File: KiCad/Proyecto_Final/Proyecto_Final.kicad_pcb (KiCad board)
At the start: 4 copper layers, 102 x 106.3 mm, 228 parts, among them J1 I2C1, J10 PA, J11 PD, J12 SPI4, J13 OutEn, J14 CLK_OUT0, J15 RF_IN, J2 ARM SWD, J3 USB_B_Micro, J4 Boot_Select, J5 PG, J6 PC, J7 PF, J8 PB, J9 PE, Q1 Si2301CDS, SW1 Reset, T1 2450BL05A0100, T2 B0310J50100AHF, T3 B0310J50100AHF, U1 MAX1193ETI+, U10 SKY13351, U11 SKY13351, U12 SKY13351, U13 SKY13351, U14 MAAL-010200, U2 MAX2837, U3 AMS1117-3.3, U4 USBLC6-2SC6, U5 STM32F723ZCTx, U6 5P49V5929, U7 SKY13351, U8 RFFC5072, U9 SKY13351, Y1 25MHz

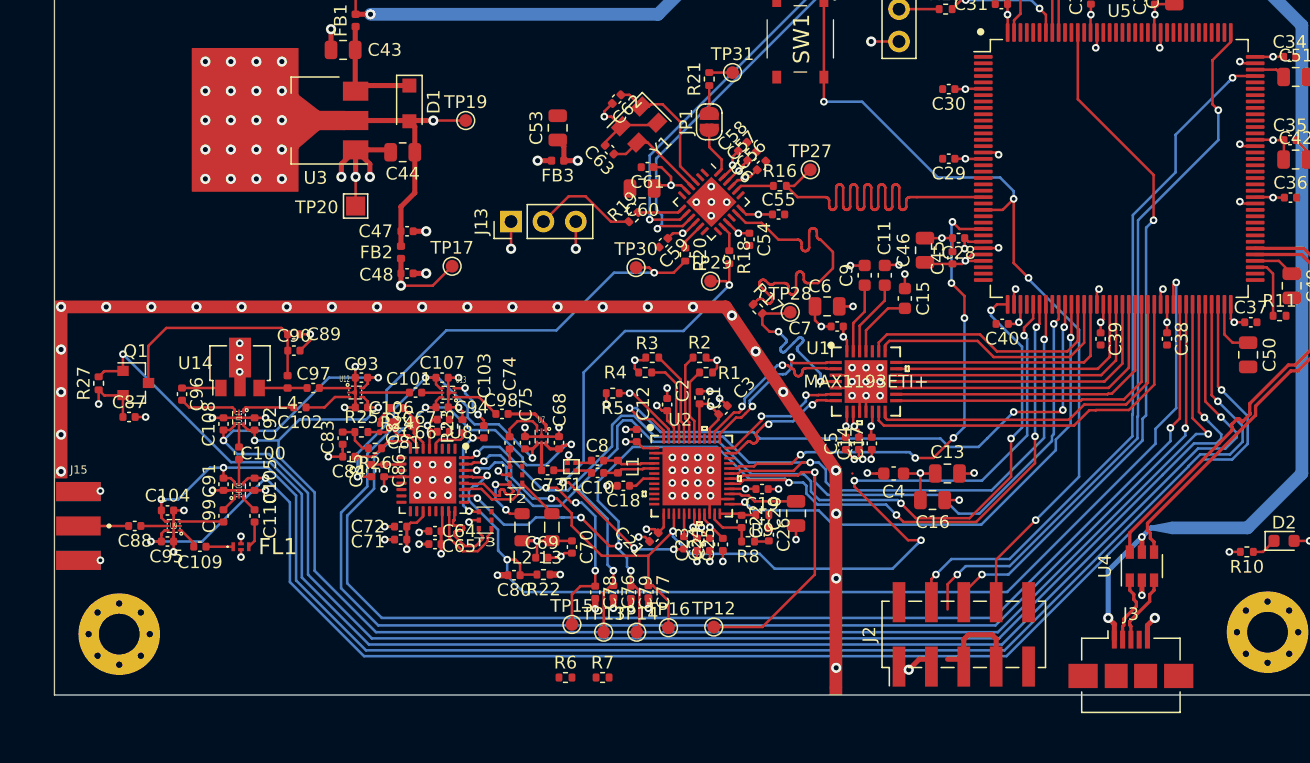
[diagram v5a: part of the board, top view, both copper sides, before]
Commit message: Pistas reacomodadas para mejor ruteo.
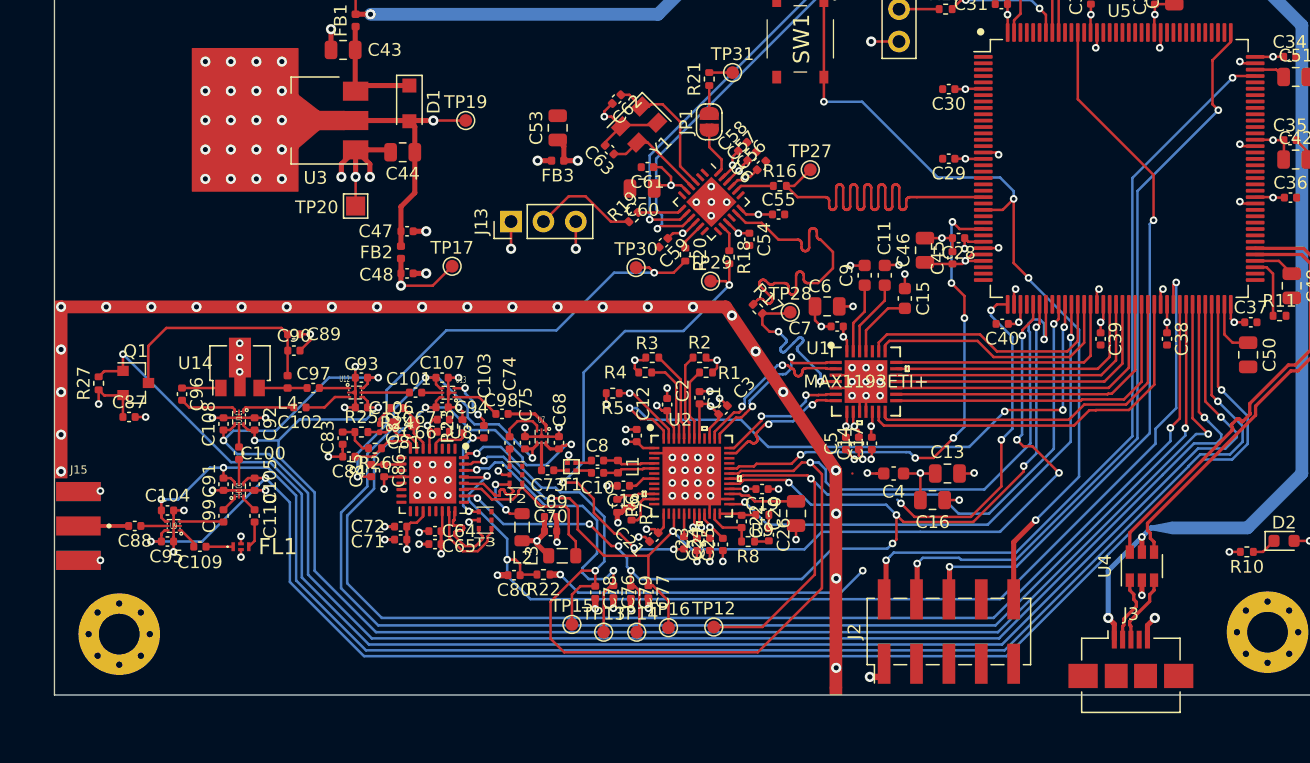
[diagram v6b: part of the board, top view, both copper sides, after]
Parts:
- moved R6 14.1 mm to (119.9, 134.4), turned to 270 degrees
- moved R7 13.1 mm to (121.0, 135.0), turned to 270 degrees
- moved C69 3.27 mm to (114.7, 135.3)
- moved L3 2.38 mm to (115.6, 138.3), turned to 0 degrees
- moved C70 2.09 mm to (114.7, 136.4), turned to 0 degrees
- moved J2 1.19 mm to (145.9, 144.3)
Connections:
- net B1 renamed PD7
- net B2 renamed PG9
- net B3 renamed PG10
- net B4 renamed PG11
- net B5 renamed PG12
- net B6 renamed PG14
- net B7 renamed PG13
- C1 pad 2: VDD -> +3.3VA
- C12 pad 2: VDD -> +3.3VA
- C13 pad 2: VDD -> +3.3VA
- C14 pad 2: VDD -> +3.3VA
- C16 pad 2: VDD -> +3V3
- C17 pad 2: VDD -> +3V3
- C18 pad 1: VDD -> +3.3VA
- C19 pad 2: VDD -> +3.3VA
- C2 pad 2: VDD -> +3.3VA
- C21 pad 1: VDD -> +3.3VA
- C23 pad 2: VDD -> +3.3VA
- C24 pad 2: VDD -> +3.3VA
- C25 pad 2: VDD -> +3.3VA
- C28 pad 1: VDD -> +3V3
- C29 pad 1: VDD -> +3V3
- C3 pad 2: VDD -> +3.3VA
- C30 pad 1: VDD -> +3V3
- C31 pad 1: VDD -> +3V3
- C32 pad 1: VDD -> +3V3
- C33 pad 1: VDD -> +3V3
- C34 pad 1: VDD -> +3V3
- C35 pad 1: VDD -> +3V3
- C36 pad 1: VDD -> +3V3
- C37 pad 1: VDD -> +3V3
- C38 pad 1: VDD -> +3V3
- C39 pad 1: VDD -> +3V3
- C4 pad 2: VDD -> +3.3VA
- C40 pad 1: VDD -> +3V3
- C41 pad 1: VDD -> +3V3
- C42 pad 1: VDD -> +3V3
- C44 pad 1: VDD -> +3V3
- C47 pad 1: VDD -> +3V3
- C5 pad 2: VDD -> +3.3VA
- C6 pad 1: VDD -> +3.3VA
- C7 pad 1: VDD -> +3.3VA
- C71 pad 1: VDD -> +3.3VA
- C72 pad 1: VDD -> +3.3VA
- C87 pad 1: VDD -> +3.3VA
- D1 pad 2: VDD -> +3V3
- D2 pad 2: VDD -> +3V3
- FB2 pad 1: VDD -> +3V3
- FB3 pad 2: VDD -> +3V3
- J13 pad 1: VDD -> +3V3
- J2 pad 1: VDD -> +3V3
- J4 pad 1: VDD -> +3V3
- Q1 pad 2: VDD -> +3.3VA
- R14 pad 1: VDD -> +3V3
- R22 pad 1: VDD -> +3V3
- R27 pad 1: VDD -> +3.3VA
- TP19 pad 1: VDD -> +3V3
- U1 pad 12: VDD -> +3V3
- U1 pad 28: VDD -> +3.3VA
- U1 pad 8: VDD -> +3.3VA
- U1 pad 9: VDD -> +3.3VA
- U2 pad 1: VDD -> +3.3VA
- U2 pad 13: VDD -> +3.3VA
- U2 pad 19: VDD -> +3.3VA
- U2 pad 20: VDD -> +3.3VA
- U2 pad 21: VDD -> +3.3VA
- U2 pad 28: VDD -> +3.3VA
- U2 pad 39: VDD -> +3.3VA
- U2 pad 40: RXHP -> Net-(U2-Pad40)
- U2 pad 41: VDD -> +3.3VA
- U2 pad 46: VDD -> +3.3VA
- U2 pad 7: VDD -> +3.3VA
- U3 pad 2: VDD -> +3V3
- U5 pad 108: VDD -> +3V3
- U5 pad 121: VDD -> +3V3
- U5 pad 131: VDD -> +3V3
- U5 pad 141: RXHP -> PE0
- U5 pad 144: VDD -> +3V3
- U5 pad 17: VDD -> +3V3
- U5 pad 30: VDD -> +3V3
- U5 pad 39: VDD -> +3V3
- U5 pad 52: VDD -> +3V3
- U5 pad 6: VDD -> +3V3
- U5 pad 62: VDD -> +3V3
- U5 pad 72: VDD -> +3V3
- U5 pad 86: VDD -> +3V3
- U5 pad 95: VDD -> +3V3
- U8 pad 19: VDD -> +3.3VA
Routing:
- net VDD: track 108.0 -> 0.00 mm, vias 57 -> 19
- net +3V3: track 0.00 -> 89.3 mm, vias 0 -> 24
- net SPI1_CS0: track 82.8 -> 51.5 mm
- net SPI1_MOSI: track 87.3 -> 107.2 mm, vias 6 -> 4
- net +3.3VA: track 136.2 -> 147.6 mm, vias 6 -> 22
- net GND: track 159.9 -> 152.5 mm
- net SPI1_SCK: track 84.7 -> 78.5 mm
- net /Frontend_analog/MIX_OPN: track 9.12 -> 14.3 mm
- net SWDIO: track 56.0 -> 59.7 mm
- net Net-(R7-Pad2): track 0.00 -> 3.15 mm
- net Net-(R6-Pad1): track 0.00 -> 3.07 mm
- net SWCLK: track 56.9 -> 59.5 mm
- net SWO: track 55.1 -> 56.6 mm
- net NRST: track 68.7 -> 67.3 mm
- net SPI1_CS1: track 58.3 -> 57.3 mm
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
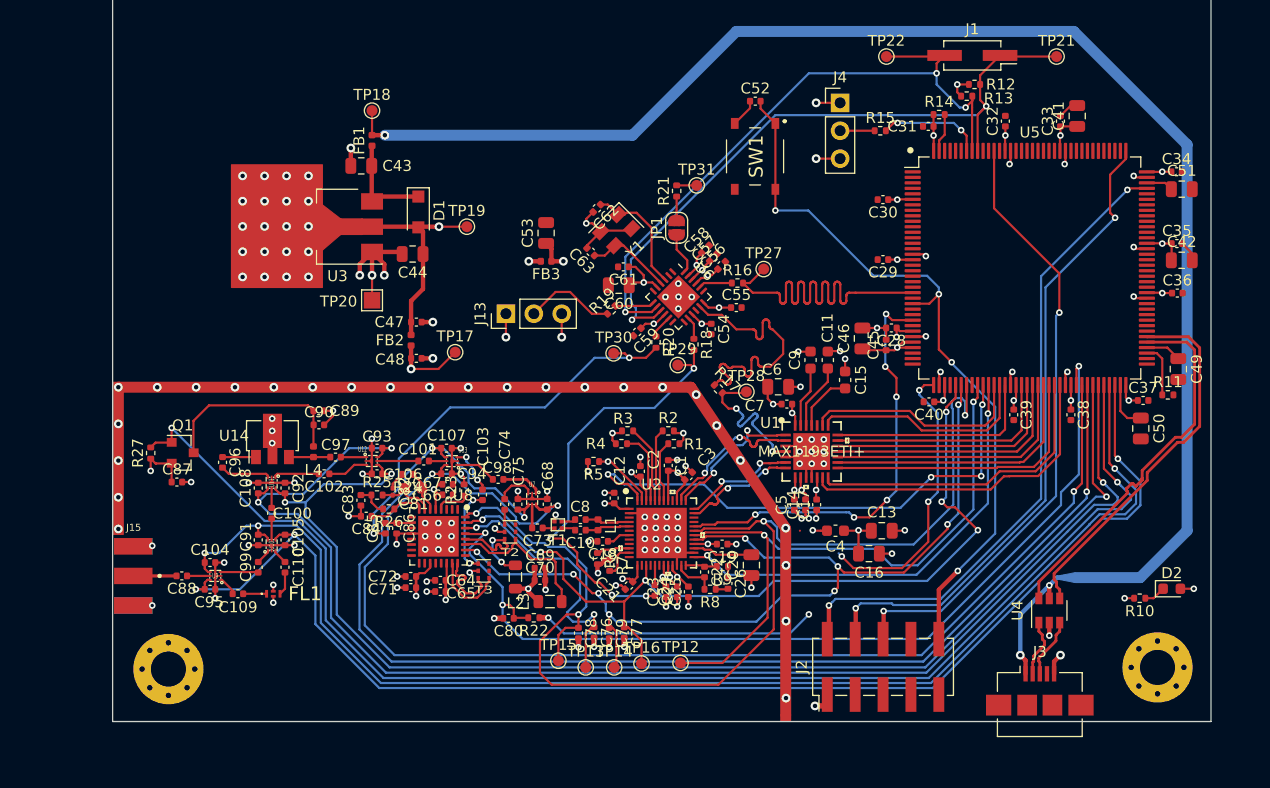
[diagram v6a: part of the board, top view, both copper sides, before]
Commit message: Avances PCBv2.
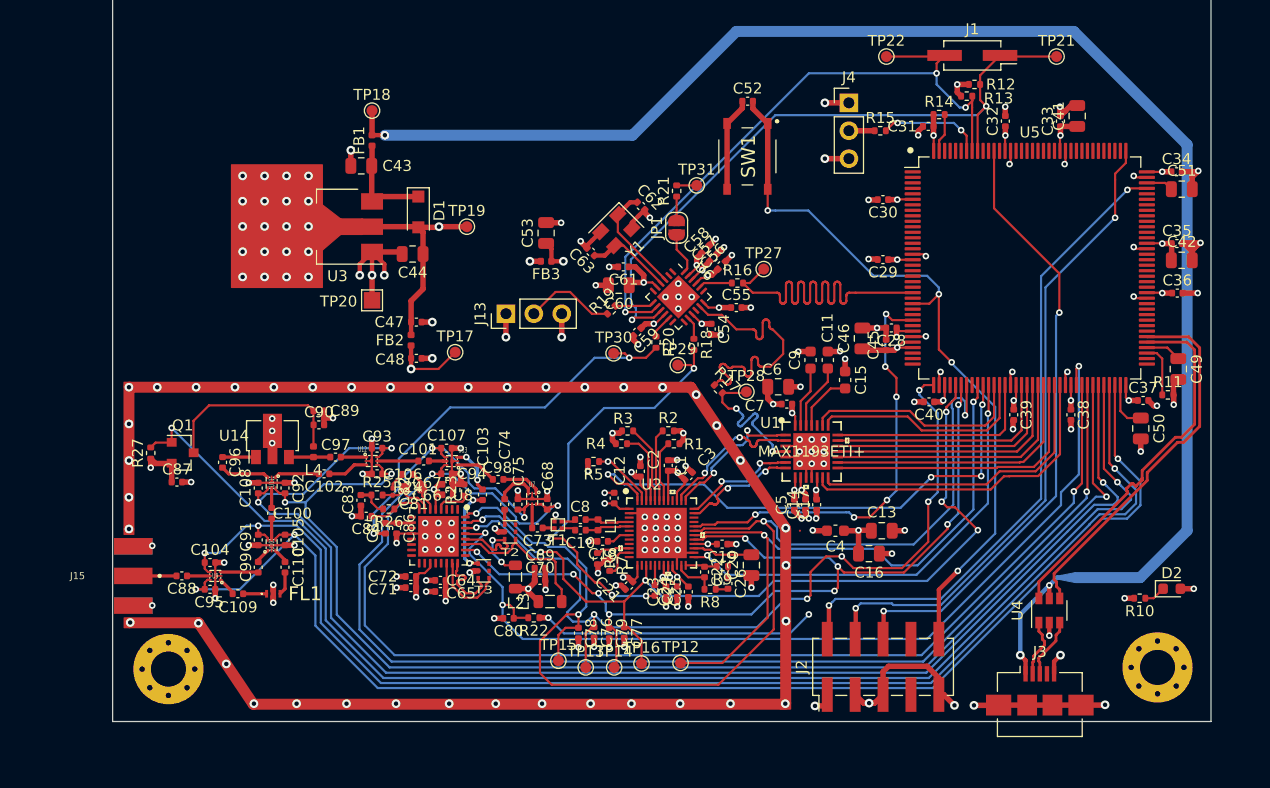
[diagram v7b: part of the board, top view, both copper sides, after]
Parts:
- moved C62 4.02 mm to (123.9, 102.3), turned to 315 degrees
- moved J4 0.80 mm to (142.8, 92.9)
- moved C52 0.70 mm to (133.6, 92.8)
- moved SW1 0.70 mm to (133.5, 97.8)
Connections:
- J3 pad 6: Net-(J3-Pad6) -> GND
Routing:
- net GND: track 152.5 -> 223.9 mm, vias 147 -> 189
- net SPI1_CS0: track 51.5 -> 78.0 mm, vias 5 -> 6
- net +3.3VA: track 147.6 -> 154.2 mm
- net XOUT: track 10.9 -> 9.91 mm
- net Net-(J4-Pad2): track 3.15 -> 2.35 mm
- net NRST: track 67.3 -> 68.0 mm
- net SPI1_MISO: track 85.6 -> 85.1 mm

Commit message: Avances PCB.
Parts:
- removed the TP2 at (197.9, 59.4)
- removed the TP21 at (161.7, 88.7)
- removed the TP22 at (146.2, 88.7)
- removed the TP23 at (205.5, 64.5)
- removed the TP24 at (228.4, 49.3)
- removed the TP25 at (213.2, 69.6)
- removed the TP26 at (205.5, 59.4)
- removed the TP3 at (190.3, 64.5)
- removed TP32: TestPoint, TestPoint:TestPoint_Pad_D1.0mm
- removed the TP4 at (197.9, 54.4)
- removed the TP5 at (197.9, 49.3)
- removed the TP6 at (190.3, 54.4)
- removed the TP7 at (197.9, 69.6)
- removed the TP8 at (197.9, 64.5)
- removed the TP9 at (190.3, 49.3)
- added J16: Conn_01x06, Connector_PinHeader_2.54mm:PinHeader_1x06_P2.54mm_Vertical, F.Cu at (169.8, 71.1)
- J10: footprint Connector_PinHeader_2.54mm:PinHeader_2x06_P2.54mm_Vertical_SMD -> Connector_PinHeader_2.54mm:PinHeader_2x05_P2.54mm_Vertical_SMD
- J11: value PD -> SPI4; footprint Connector_PinHeader_2.54mm:PinHeader_2x08_P2.54mm_Vertical_SMD -> Connector_PinHeader_2.54mm:PinHeader_1x04_P2.54mm_Vertical_SMD_Pin1Left
- J12: value SPI4 -> PD; footprint Connector_PinHeader_2.54mm:PinHeader_1x04_P2.54mm_Vertical_SMD_Pin1Left -> Connector_PinHeader_2.54mm:PinHeader_2x08_P2.54mm_Vertical
- J5, J7: footprint Connector_PinHeader_2.54mm:PinHeader_2x03_P2.54mm_Vertical_SMD -> Connector_PinHeader_2.54mm:PinHeader_2x06_P2.54mm_Vertical_SMD
- J6: footprint Connector_PinHeader_2.54mm:PinHeader_2x06_P2.54mm_Vertical_SMD -> Connector_PinHeader_2.54mm:PinHeader_2x07_P2.54mm_Vertical_SMD
- J8: footprint Connector_PinHeader_2.54mm:PinHeader_2x04_P2.54mm_Vertical_SMD -> Connector_PinHeader_2.54mm:PinHeader_2x03_P2.54mm_Vertical_SMD
- J9: footprint Connector_PinHeader_2.54mm:PinHeader_2x04_P2.54mm_Vertical_SMD -> Connector_PinHeader_2.54mm:PinHeader_2x02_P2.54mm_Vertical_SMD
- TP1: footprint TestPoint:TestPoint_Pad_D1.0mm -> Tesis2020-21:TestPoint_Mask_D0.4mm
- TP2: renamed from TP10; footprint TestPoint:TestPoint_Pad_D1.0mm -> Tesis2020-21:TestPoint_Mask_D0.4mm
- TP3: renamed from TP11; footprint TestPoint:TestPoint_Pad_D1.0mm -> Tesis2020-21:TestPoint_Mask_D0.4mm
- moved TP20 164.3 mm to (80.1, 121.5)
- moved TP23 160.7 mm to (93.6, 133.9)
- moved TP22 152.8 mm to (85.2, 132.9)
- moved TP21 144.0 mm to (87.5, 129.3)
- moved TP18 143.8 mm to (92.8, 130.0)
- moved J11 131.7 mm to (134.6, 97.6)
- moved TP25 127.9 mm to (119.6, 127.5)
- moved TP24 123.7 mm to (117.0, 128.4)
- moved TP19 111.3 mm to (105.2, 122.8)
- moved TP3 80.7 mm to (143.5, 125.2)
- moved TP26 79.8 mm to (140.4, 137.0)
- moved J9 75.1 mm to (138.9, 79.0)
- moved J7 71.7 mm to (116.9, 82.5)
- moved TP2 68.6 mm to (144.8, 121.0)
- moved TP1 65.5 mm to (142.7, 121.5)
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- renumbered C71 to C68, C72 to C69, C68 to C70, C69 to C71, C70 to C72, TP18 to TP10, TP19 to TP11, TP20 to TP12, TP27 to TP13, TP28 to TP14, TP29 to TP15, TP30 to TP16, TP31 to TP17, TP33 to TP18, TP34 to TP19, TP35 to TP20, TP36 to TP21, TP37 to TP22, TP38 to TP23, TP39 to TP24, TP40 to TP25, TP41 to TP26, TP12 to TP4, TP13 to TP5, TP14 to TP6, TP15 to TP7, TP16 to TP8, TP17 to TP9
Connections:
- net PE11 renamed Net-(J9-Pad4)
- J10 pad 10: PA12 -> PA15
- J10 pad 4: PC4 -> PA4
- J10 pad 5: PA4 -> Net-(J10-Pad5)
- J10 pad 6: PA8 -> Net-(J10-Pad6)
- J10 pad 7: PA9 -> Net-(J10-Pad7)
- J10 pad 8: PA10 -> Net-(J10-Pad8)
- J10 pad 9: PA11 -> Net-(J10-Pad9)
- J11 pad 1: PD0 -> SPI4_SCK
- J11 pad 2: PD1 -> SPI4_CS
- J11 pad 3: PD2 -> SPI4_MISO
- J11 pad 4: PD3 -> SPI4_MOSI
- J12 pad 1: SPI4_SCK -> PD8
- J12 pad 2: SPI4_MOSI -> PC8
- J12 pad 3: SPI4_MISO -> PD9
- J12 pad 4: SPI4_CS -> PC7
- J5 pad 1: PG2 -> Net-(J5-Pad1)
- J5 pad 2: PG3 -> Net-(J5-Pad2)
- J5 pad 3: PG4 -> Net-(J5-Pad3)
- J5 pad 4: PG5 -> Net-(J5-Pad4)
- J5 pad 5: PG8 -> Net-(J5-Pad5)
- J5 pad 6: PG15 -> PG9
- J6 pad 10: PC12 -> PC11
- J6 pad 11: PC14 -> PC12
- J6 pad 12: PC15 -> PC13
- J6 pad 4: PC6 -> PC4
- J6 pad 5: PC7 -> Net-(J6-Pad5)
- J6 pad 6: PC8 -> Net-(J6-Pad6)
- J6 pad 7: PC9 -> Net-(J6-Pad7)
- J6 pad 8: PC10 -> Net-(J6-Pad8)
- J6 pad 9: PC11 -> PC10
- J7 pad 1: PF6 -> Net-(J7-Pad1)
- J7 pad 2: PF7 -> PF0
- J7 pad 3: PF8 -> PF10
- J7 pad 4: PF9 -> PF1
- J7 pad 5: PF10 -> PF9
- J7 pad 6: Net-(J7-Pad6) -> PF2
- J8 pad 5: PB10 -> PB12
- J8 pad 6: PB11 -> PB13
- J9 pad 1: PE1 -> PE0
- J9 pad 2: PE3 -> PE1
- J9 pad 3: PE10 -> PE3
- TP1 pad 1: D7 -> PD1_adc
- TP2 pad 1: PD0 -> PD0_adc
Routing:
- net +5V: track 144.9 -> 219.8 mm
- net PF10: track 0.00 -> 66.8 mm, vias 0 -> 2
- net PF9: track 0.00 -> 61.6 mm, vias 0 -> 2
- net PF8: track 0.00 -> 54.1 mm
- net PF7: track 0.00 -> 50.1 mm
- net PF3: track 0.00 -> 44.8 mm, vias 0 -> 2
- net PF0: track 0.00 -> 44.5 mm, vias 0 -> 2
- net PF1: track 0.00 -> 43.7 mm, vias 0 -> 2
- net PF2: track 0.00 -> 42.5 mm, vias 0 -> 2
- net PF4: track 0.00 -> 42.2 mm, vias 0 -> 2
- net PF6: track 0.00 -> 42.0 mm
- net PF5: track 0.00 -> 37.6 mm, vias 0 -> 2
- net SPI4_SCK: track 0.00 -> 19.3 mm
- net SPI4_MISO: track 0.00 -> 16.4 mm
- net SPI4_CS: track 0.00 -> 14.9 mm
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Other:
- board size 102 x 106.3 mm -> 100 x 100 mm
